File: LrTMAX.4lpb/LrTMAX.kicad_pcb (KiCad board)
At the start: 4 copper layers, 100 x 100 mm, 126 parts, among them J1 USB_C_Receptacle_USB2.0, J2 SM06B-SRSS-TB, Q1 2N7002, SW1 Tact_SW_8mm, SW10 EC11_SMD, SW11 EC11_SMD, SW12 EC11_SMD, SW13 EC11_SMD, SW14 EC11_SMD, SW15 EC11_SMD, SW16 EC11_SMD, SW17 EC11_SMD, SW2 Tact_SW_8mm, SW3 Tact_SW_8mm, SW4 Tact_SW_8mm, SW5 Tact_SW_8mm, SW6 Tact_SW_8mm, SW7 Tact_SW_8mm, SW8 Tact_SW_8mm, U1 STM32F072C8Tx, U3 SSD1306_OLED_0.91, U4 SPX3819M5-L3-3TR

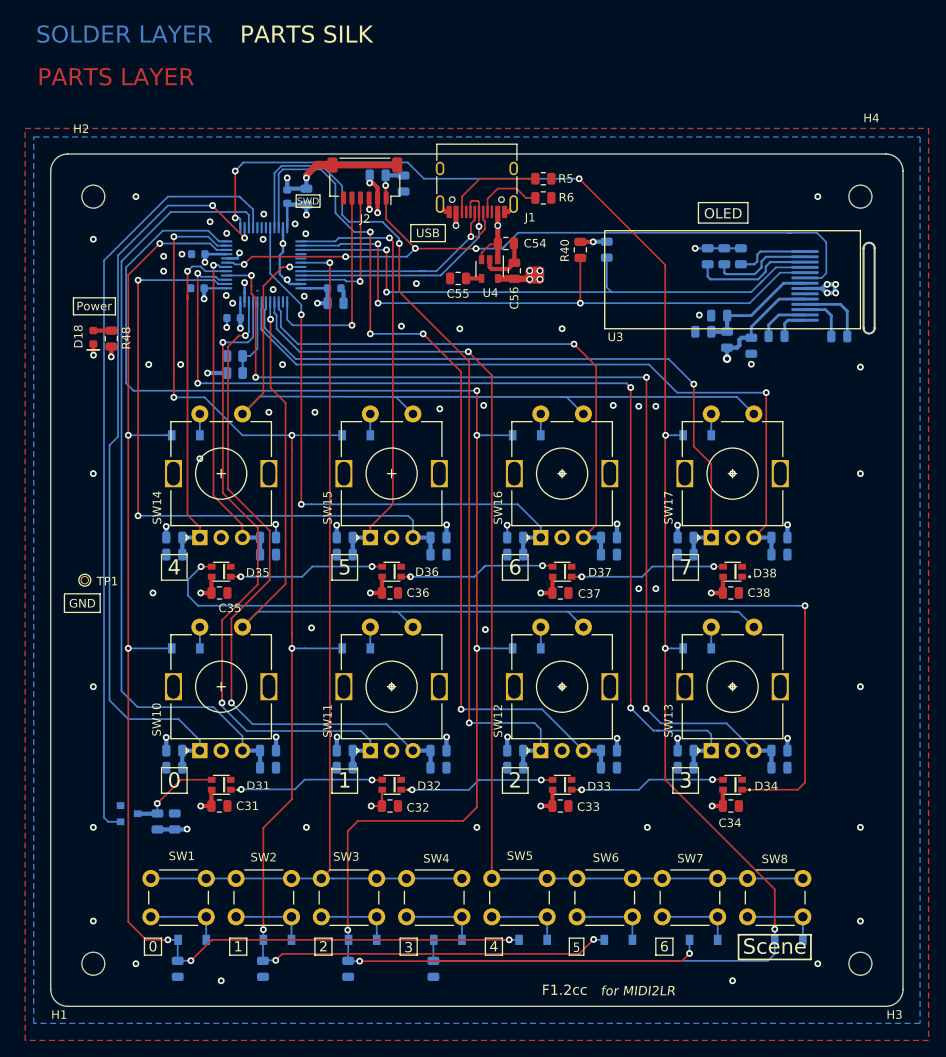
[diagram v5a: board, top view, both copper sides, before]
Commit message: replace SWD to 10p header
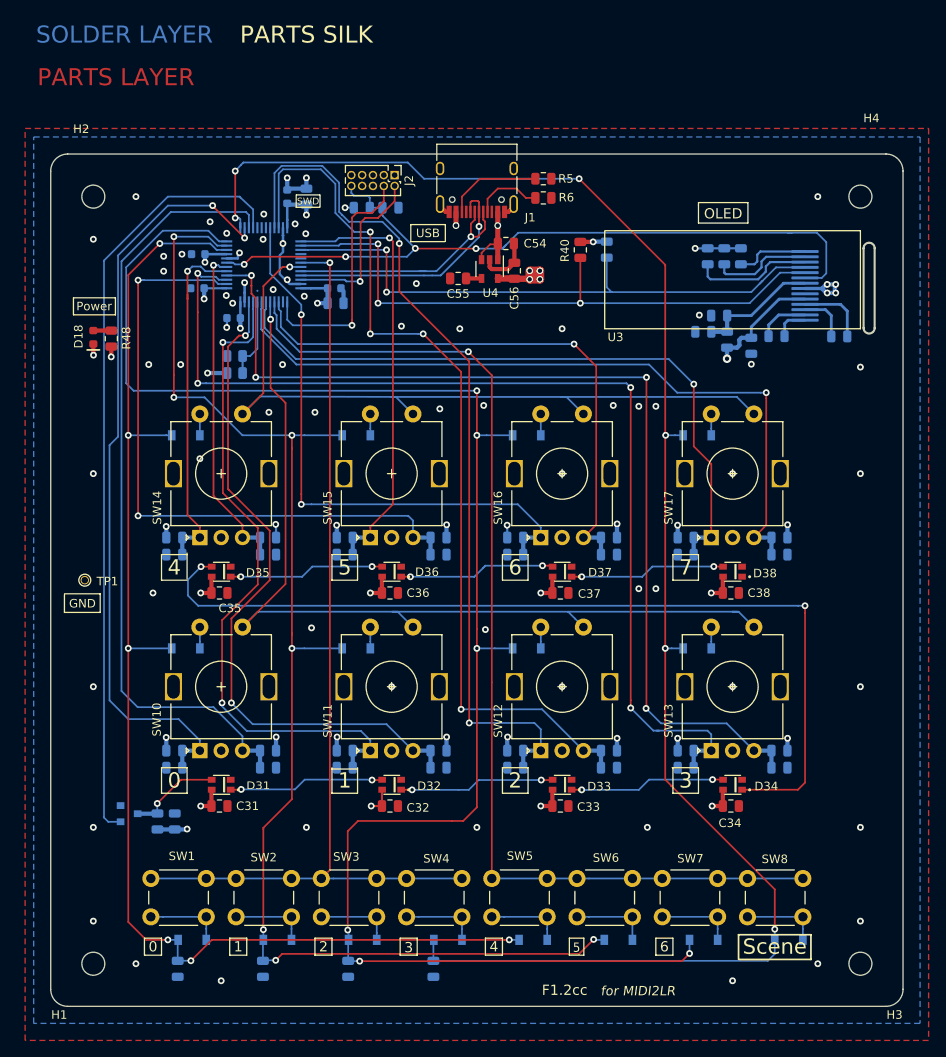
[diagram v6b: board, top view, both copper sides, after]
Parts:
- J2: value SM06B-SRSS-TB -> Conn_02x05_Odd_Even; footprint Connector_JST:JST_SH_SM06B-SRSS-TB_1x06-1MP_P1.00mm_Horizontal -> Connector_PinHeader_1.27mm:PinHeader_2x05_P1.27mm_Vertical
- moved R47 4.23 mm to (136.5, 106.3)
- moved J2 3.56 mm to (140.3, 102.5), turned to -90 degrees
- moved C53 3.23 mm to (139.9, 106.3), turned to 0 degrees
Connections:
- D38 pad 1: Net-(D38-Pad1) -> unconnected-(D38-Pad1)
- J1 pad A8: Net-(J1-PadA8) -> unconnected-(J1-PadA8)
- J1 pad B8: Net-(J1-PadB8) -> unconnected-(J1-PadB8)
- J2 pad 1: /NRST -> +3V3
- J2 pad 2: +3V3 -> /SWDIO
- J2 pad 4: /SWDIO -> /SWCLK
- J2 pad 5: /SWCLK -> GND
- J2 pad 6: Net-(J2-Pad6) -> unconnected-(J2-Pad6)
- U1 pad 17: Net-(U1-Pad17) -> unconnected-(U1-Pad17)
- U1 pad 18: Net-(U1-Pad18) -> unconnected-(U1-Pad18)
- U1 pad 19: Net-(U1-Pad19) -> unconnected-(U1-Pad19)
- U1 pad 28: Net-(U1-Pad28) -> unconnected-(U1-Pad28)
- U1 pad 29: Net-(U1-Pad29) -> unconnected-(U1-Pad29)
- U1 pad 38: Net-(U1-Pad38) -> unconnected-(U1-Pad38)
- U3 pad 6: Net-(U3-Pad6) -> unconnected-(U3-Pad6)
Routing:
- net GND: track 58.9 -> 46.4 mm, vias 73 -> 72
- net +3V3: track 84.0 -> 80.4 mm, vias 31 -> 30
- net /SWCLK: track 25.4 -> 28.9 mm
- net /SWDIO: track 17.3 -> 20.8 mm
- net /NRST: track 92.4 -> 92.3 mm, vias 5 -> 4
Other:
- net class Default removed
- net class GND removed
- net class VBUS removed
- net class VCC removed

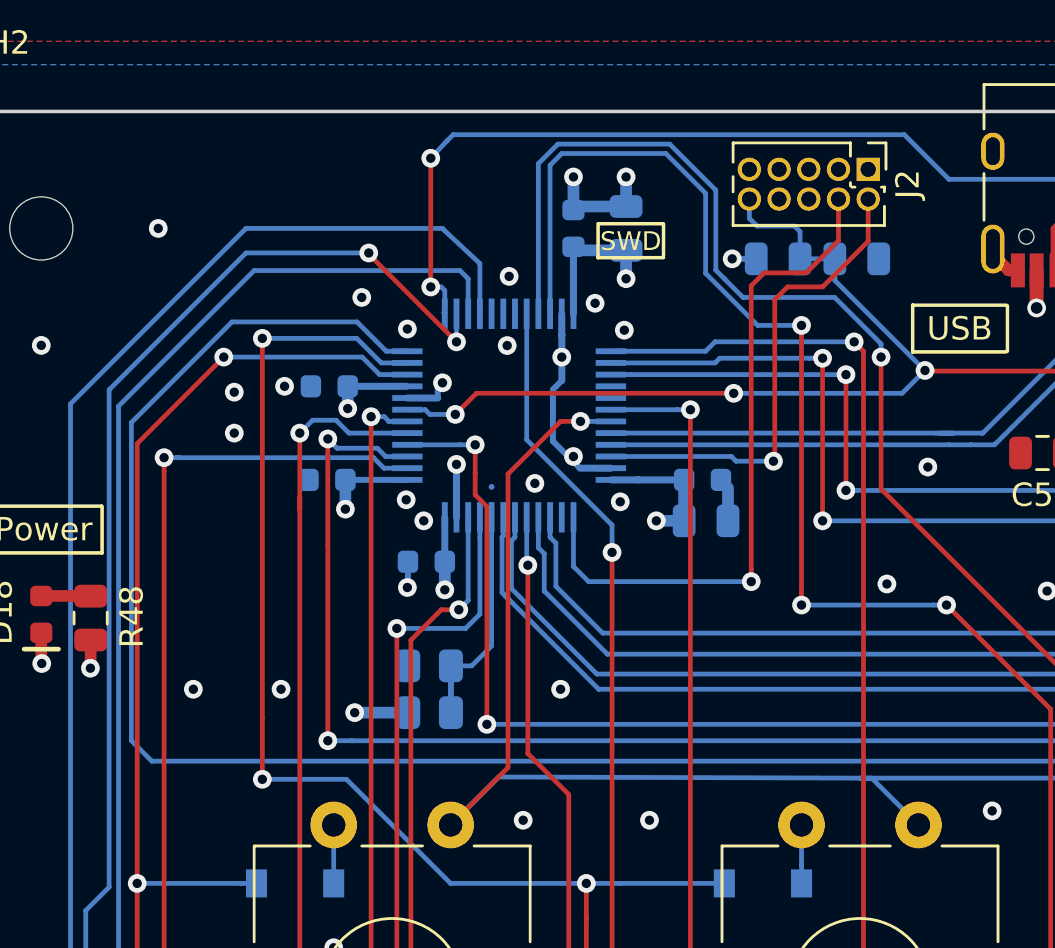
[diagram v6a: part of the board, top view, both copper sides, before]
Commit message: Added DFU DIP Switch.
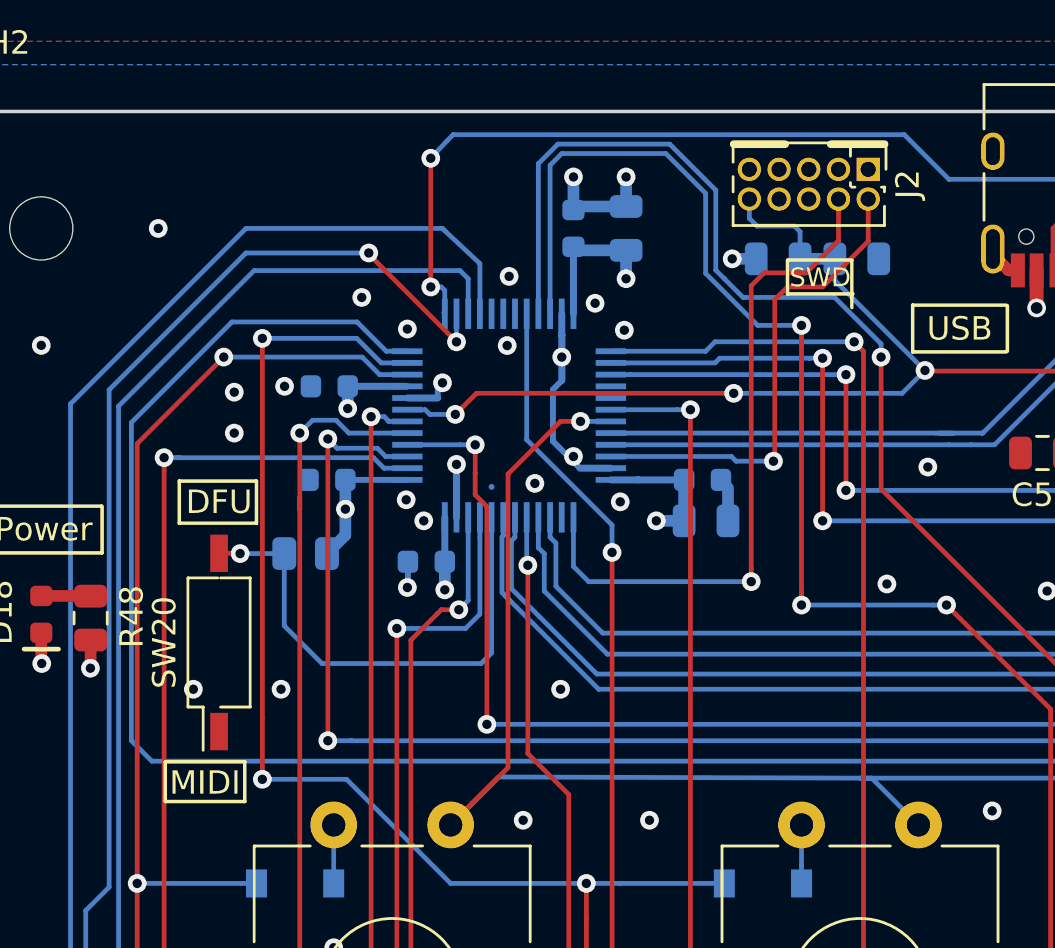
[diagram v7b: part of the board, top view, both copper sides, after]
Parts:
- removed R8: 0, Resistor_SMD:R_0805_2012Metric
- added SW20: SW_SPST, Button_Switch_SMD:SW_DIP_SPSTx01_Slide_Copal_CHS-01B_W7.62mm_P1.27mm, F.Cu at (112.6, 122.7)
- moved R7 8.62 mm to (116.3, 118.9), turned to 180 degrees
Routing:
- net Net-(R7-Pad2): track 9.59 -> 21.4 mm, vias 0 -> 1
- net +3V3: vias 30 -> 29
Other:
- board text added: "DFU"
- board text added: "MIDI"
